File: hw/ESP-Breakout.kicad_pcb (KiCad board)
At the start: 2 copper layers, 50.8 x 20.3 mm, 16 parts, among them M1 ESP-07, P1 FTDI BASIC, P2 CONN_01X11, P3 CONN_01X11, Q1 BSS138, Q2 BSS138, SW1 SW_PUSH, U1 1117-3.3

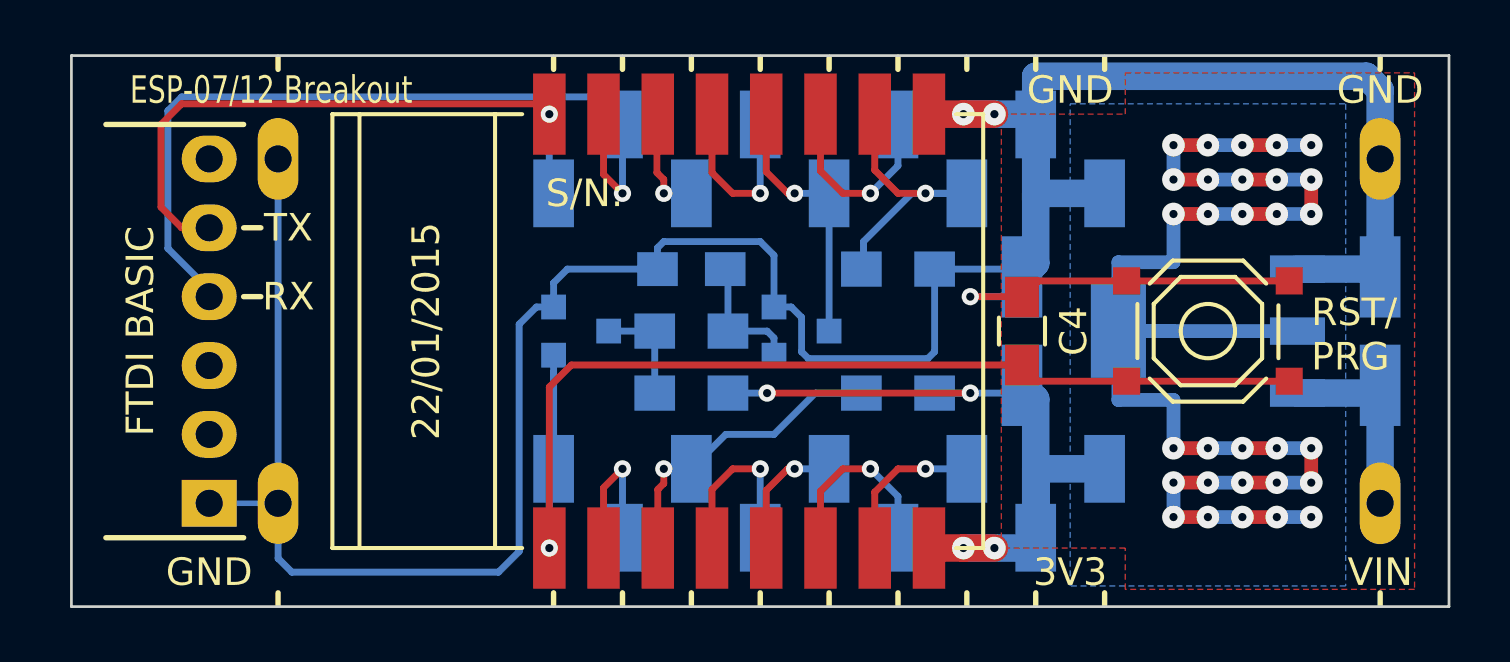
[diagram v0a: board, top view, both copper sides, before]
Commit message: Footprint change
Footprint change to facilitate hand soldering
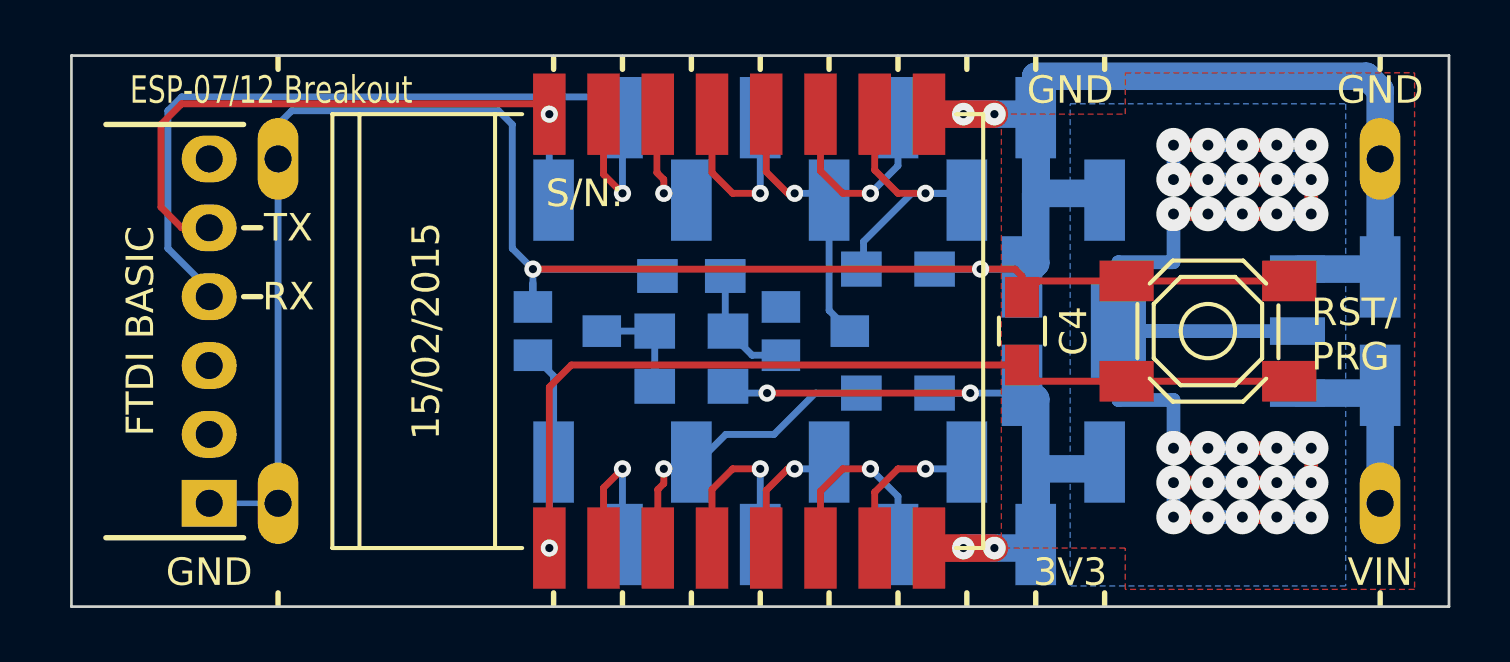
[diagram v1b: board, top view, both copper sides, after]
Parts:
- moved Q1 0.51 mm to (125.0, 128.3)
- moved Q2 0.51 mm to (134.1, 128.3)
- moved R1 0.25 mm to (129.5, 130.3)
- moved C1 0.25 mm to (129.5, 126.2)
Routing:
- net GND: track 119.2 -> 113.4 mm, vias 3 -> 4
- net /RESET: track 45.0 -> 41.3 mm
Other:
- board text added: "15/02/2015"
- board text removed: "22/01/2015"

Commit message: Minor footprint change to Tantalum caps
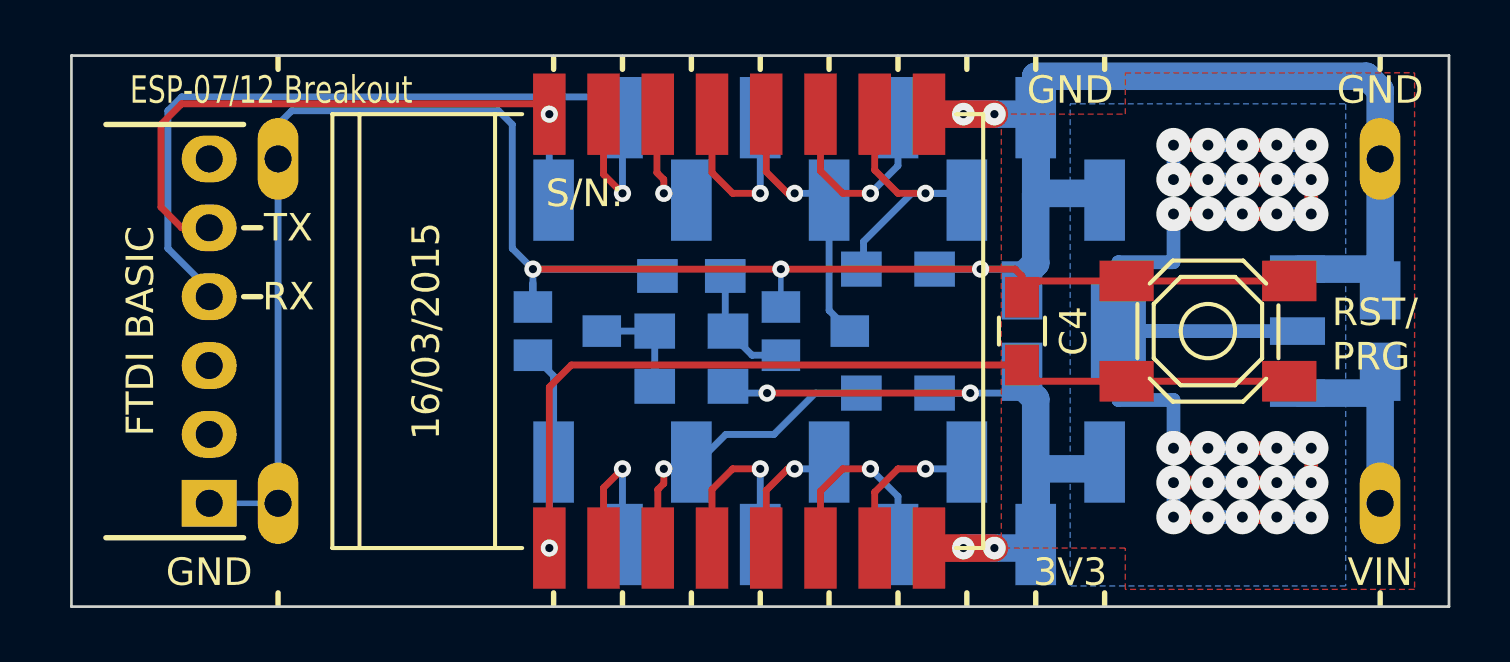
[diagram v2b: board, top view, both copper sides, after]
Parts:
- C2, C3: footprint Capacitors_Tantalum_SMD:TantalC_SizeA_EIA-3216_HandSoldering -> Capacitors_Tantalum_SMD:TantalC_SizeA_EIA-3216_Wave
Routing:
- net GND: track 113.4 -> 114.8 mm, vias 4 -> 5
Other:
- board text added: "16/03/2015"
- board text removed: "15/02/2015"

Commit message: V1.1
Added a pull-up resistor on GPIO0 pin
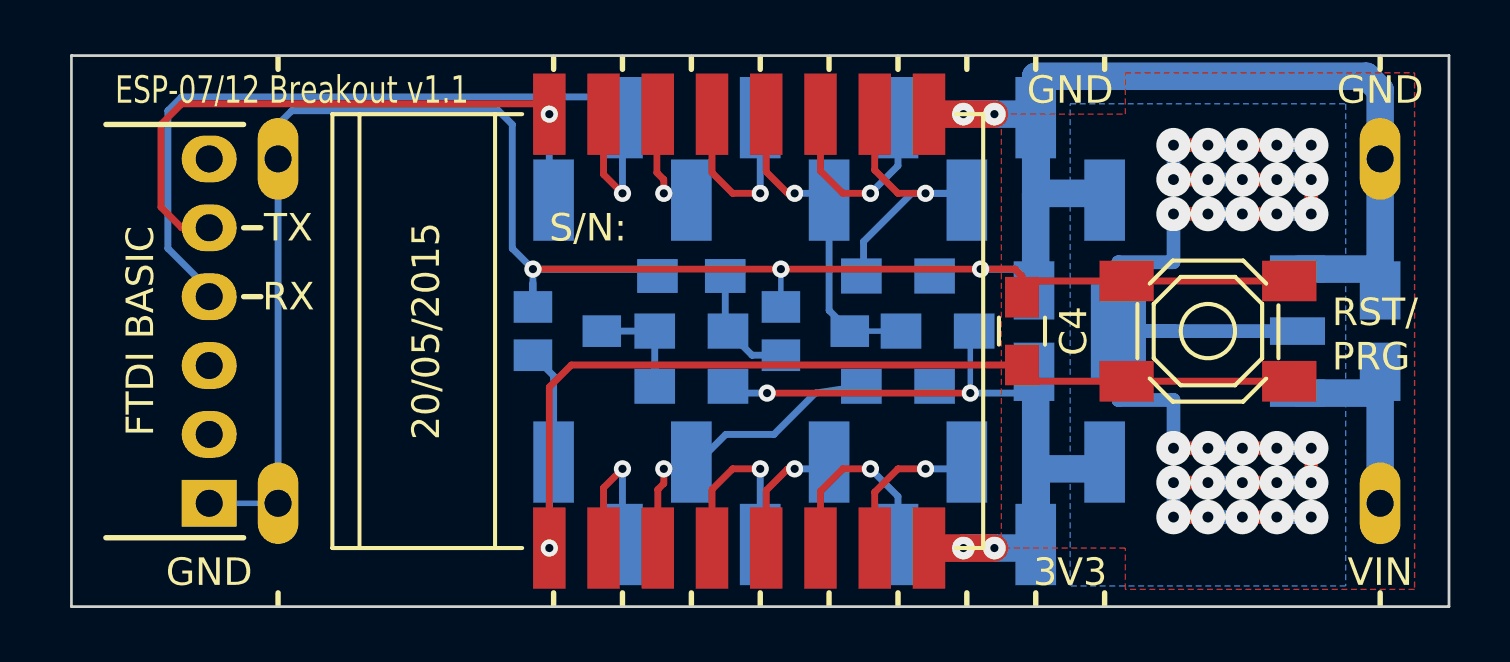
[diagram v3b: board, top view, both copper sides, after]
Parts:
- added R5: 10K, Resistors_SMD:R_0805_HandSoldering, B.Cu at (138.6, 128.3)
- C3: value 10u -> 22u
- moved C3 0.44 mm to (142.2, 128.3)
- moved R4 0.25 mm to (137.2, 130.3)
- moved R3 0.25 mm to (137.2, 126.2)
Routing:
- net /GPIO0: track 9.92 -> 11.8 mm
- net +3V3: track 85.0 -> 86.8 mm
- net GND: track 114.8 -> 114.2 mm
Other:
- board text added: "20/05/2015"
- board text added: "ESP-07/12 Breakout v1.1"
- board text removed: "16/03/2015"
- board text removed: "ESP-07/12 Breakout"
